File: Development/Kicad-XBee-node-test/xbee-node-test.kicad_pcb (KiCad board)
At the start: 2 copper layers, 90 x 50 mm, 46 parts, among them IC1 ATMEGA48-P, P1 CONN_01X06, P2 CONN_01X02, P3 CONN_01X02, P4 CONN_01X02, Q1 2N7002, Q2 BSS84, SW1 Reset, SW2 Commissioning, U1 TPS77033

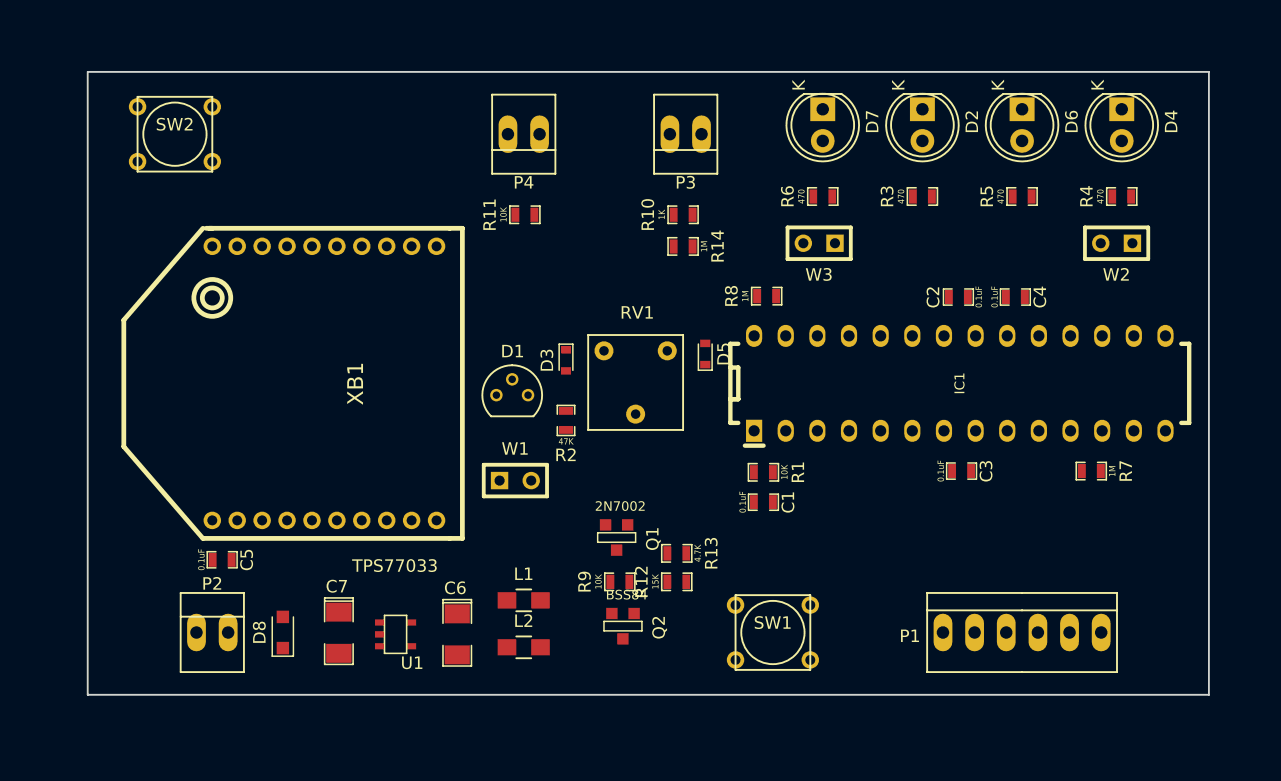
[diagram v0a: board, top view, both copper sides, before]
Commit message: Kicad-Xbee-node-test: first draft of PCB
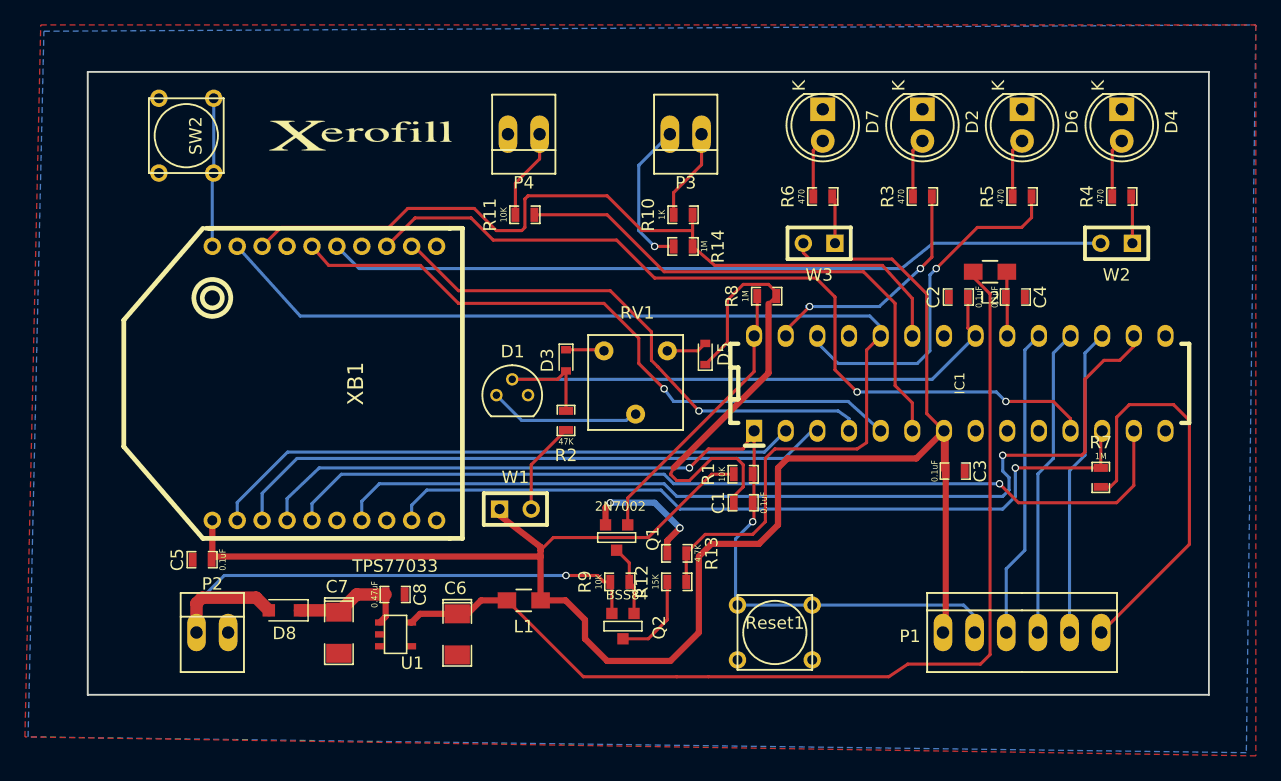
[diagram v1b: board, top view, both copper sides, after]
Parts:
- removed SW1: Reset, photodiode:SW_PUSH_TINY
- added C8: 0.47uF, photodiode:SM0603_Capa, F.Cu at (74.7, 91.9)
- added G***: LOGO, photodiode:Xerofill-Logo, F.Cu at (71.9, 55.1)
- added Reset1: Reset, photodiode:SW_PUSH_TINY, F.Cu at (105.2, 95.0)
- D2: value Green LED -> Test
- D4: value Yellow LED -> Associate
- D6: value Orange LED -> Debug
- D7: value Red LED -> Power
- D8: value D_Schottky -> CUS520
- P1: value CONN_01X06 -> Program
- P2: value CONN_01X02 -> Power 3.7V-12V
- P3: value CONN_01X02 -> Analogue
- P4: value CONN_01X02 -> Count
- moved L2 48.1 mm to (122.4, 66.0), turned to 180 degrees
- moved W1 2.29 mm to (84.3, 85.1)
- moved D8 1.79 mm to (65.8, 93.2), turned to 180 degrees
- moved R1 1.63 mm to (102.6, 82.3), turned to 0 degrees
- moved C1 1.62 mm to (102.6, 84.6), turned to 180 degrees
- moved C5 1.61 mm to (59.2, 89.2), turned to 180 degrees
- moved SW2 0.92 mm to (57.9, 55.1), turned to 270 degrees
- moved R7 0.92 mm to (131.3, 82.5), turned to 270 degrees
- moved C3 0.51 mm to (119.6, 82.0)
- turned L1 to 180 degrees
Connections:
- W3 pad 2: Net-(W3-Pad2) -> /Vcc
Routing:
- net /Vcc: track 0.00 -> 148.9 mm
- net GND: track 0.00 -> 95.3 mm, vias 0 -> 3
- net /VBAT: track 0.00 -> 87.6 mm
- net Net-(C6-Pad1): track 0.00 -> 81.6 mm
- net /MC_Reset: track 0.00 -> 77.2 mm, vias 0 -> 2
- net /Bootloader: track 0.00 -> 76.1 mm, vias 0 -> 1
- net /XBee_Reset: track 0.00 -> 74.2 mm, vias 0 -> 1
- net /On_Sleep: track 0.00 -> 66.9 mm, vias 0 -> 2
- net /Analogue: track 0.00 -> 65.1 mm
- net /Sleep_RQ: track 0.00 -> 63.4 mm, vias 0 -> 1
- net /Associate: track 0.00 -> 62.8 mm
- net /RTS: track 0.00 -> 53.1 mm, vias 0 -> 1
- net /ARef: track 0.00 -> 49.8 mm
- net /TxD: track 0.00 -> 48.8 mm
- net /Battery: track 0.00 -> 48.1 mm, vias 0 -> 1
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- added copper zone on B.Cu, net GND
- added copper zone on F.Cu, net GND
